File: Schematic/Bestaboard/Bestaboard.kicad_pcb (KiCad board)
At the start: 4 copper layers, 60 x 88 mm, 30 parts, among them J1 S5B-XH-A, J2 S5B-XH-A, J3 PPTC051LGBN-RC, J5 PPTC061LGBN-RC, J6 PRPC006SGAN-M71RC, J7 S3B-XH-A, J8 S3B-XH-A, J9 PRPC005SGAN-M71RC, U1 CD74HCT164E, U10 SN74HC32N, U2 CD4042BE, U3 CD4042BE, U4 SN74HC00N, U5 CD4081BE, U8 ULN2003APG, U9 ULN2003APG

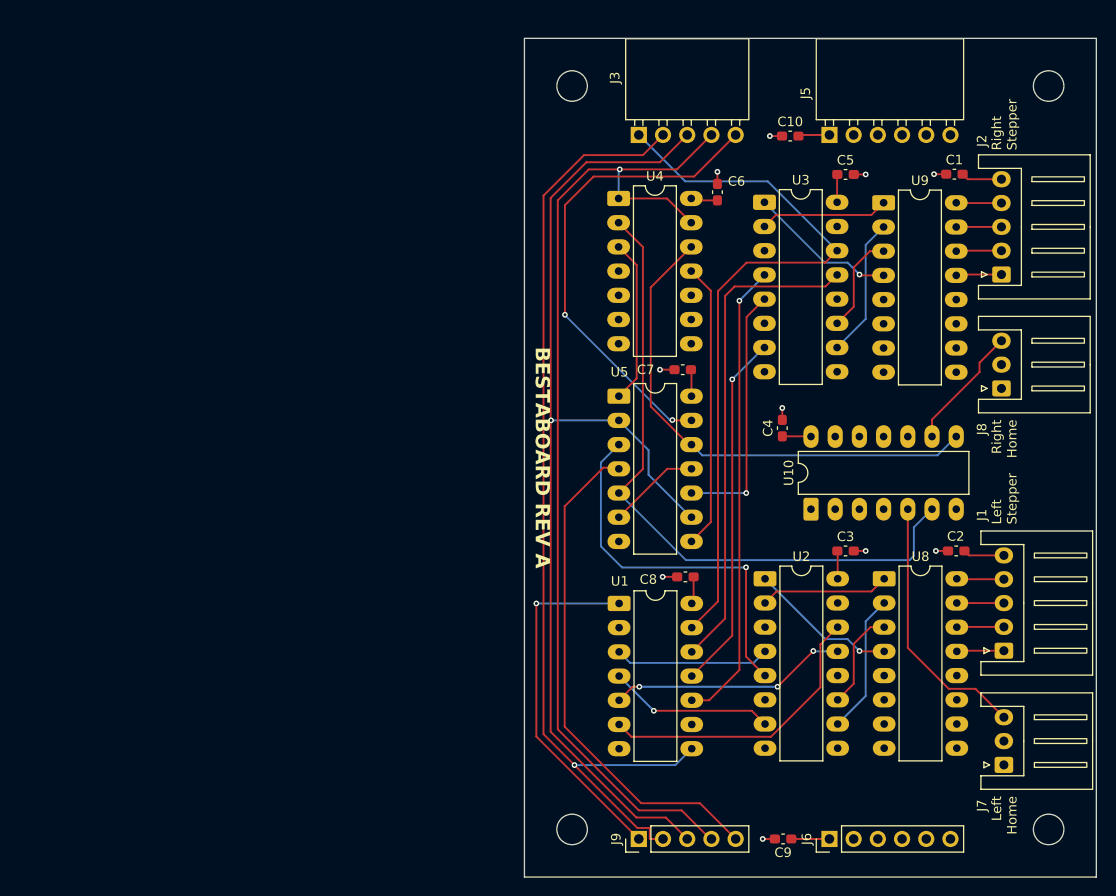
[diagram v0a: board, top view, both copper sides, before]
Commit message: Prints, Schematic, PCB, Code Update
Prints - Created print plates for flips, drum and frame, updated frame to have mounting holes on the bottom.
PCB/Schematic - Changed to 14 pin NAND chip, updated parameters.
Code - Changed code to alternate between homing and character rotation.
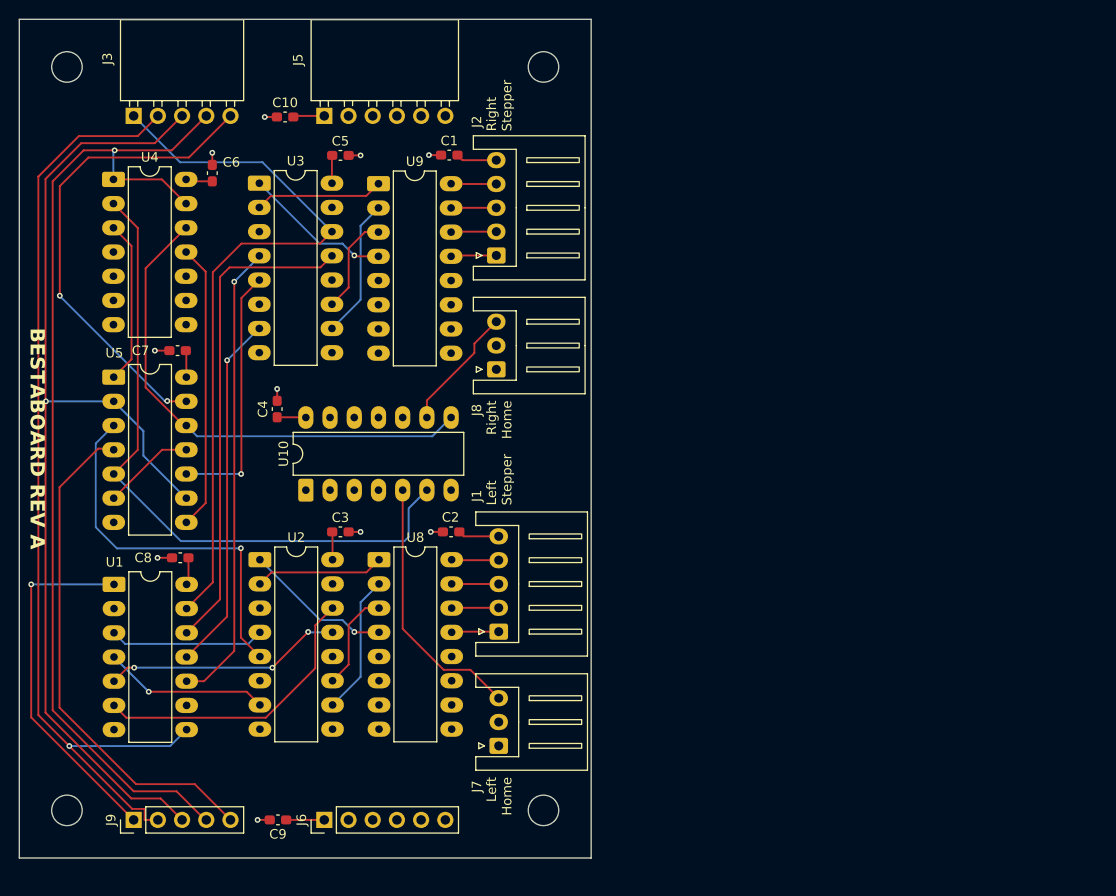
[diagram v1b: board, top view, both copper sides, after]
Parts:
- U10: value SN74HC32N -> TC74HC04APF
- U8, U9: value ULN2003APG -> ULN2003A
- moved C1 53.0 mm to (95.1, 64.2)
- moved J2 53.0 mm to (100.0, 74.8)
- moved J8 53.0 mm to (100.0, 86.7)
- moved C2 53.0 mm to (95.3, 103.8)
- moved C3 53.0 mm to (83.7, 103.8)
- moved C4 53.0 mm to (77.1, 90.9)
- moved C5 53.0 mm to (83.7, 64.3)
- moved C6 53.0 mm to (70.2, 66.1)
- moved C7 53.0 mm to (66.6, 84.8)
- moved C8 53.0 mm to (66.9, 106.5)
- moved H1 53.0 mm to (55.0, 55.0)
- moved H2 53.0 mm to (105.0, 55.0)
- moved H3 53.0 mm to (105.0, 133.0)
- moved H4 53.0 mm to (55.0, 133.0)
- moved J1 53.0 mm to (100.3, 114.2)
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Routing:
- added copper zone on In2.Cu, net +5V
- added copper zone on In1.Cu, net GND
- removed copper zone on In1.Cu, net +5V
- removed copper zone on In2.Cu, net GND
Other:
- board text added: "0"
- board text added: "0 mm"
- board text added: "0.0000 mm / 0.0000 mm"
- board text added: "0.01 mm"
- board text added: "0.02"
- board text added: "0.035 mm"
- board text added: "0.1 mm"
- board text added: "0.3000 mm"
- board text added: "1"
- board text added: "1.24 mm"
- board text added: "1.6000 mm"
- board text added: "3.3"
- board text added: "4"
- board text added: "4.5"
- board text added: "60.0000 mm x 88.0000 mm"
- board text added: "B.Cu"
- board text added: "B.Mask"
- board text added: "B.Paste"
- board text added: "B.Silkscreen"
- board text added: "BOARD CHARACTERISTICS"
- board text added: "Board Thickness:"
- board text added: "Board overall dimensions:"
- board text added: "Bottom Silk Screen"
- board text added: "Bottom Solder Mask"
- board text added: "Bottom Solder Paste"
- board text added: "Castellated pads:"
- board text added: "Color"
- board text added: "Copper Finish:"
- board text added: "Copper Layer Count:"
- board text added: "Dielectric"
- board text added: "Edge card connectors:"
- board text added: "Epsilon R"
- board text added: "F.Cu"
- board text added: "F.Mask"
- board text added: "F.Paste"
- board text added: "F.Silkscreen"
- board text added: "FR4"
- board text added: "FR4 natural"
- board text added: "Green"
- board text added: "Impedance Control:"
- board text added: "In1.Cu"
- board text added: "In2.Cu"
- board text added: "Layer Name"
- board text added: "Loss Tangent"
- board text added: "Material"
- board text added: "Min hole diameter:"
- board text added: "Min track/spacing:"
- board text added: "No"
- board text added: "None"
- board text added: "Not specified"
- board text added: "Plated Board Edge:"
- board text added: "Thickness (mm)"
- board text added: "Top Silk Screen"
- board text added: "Top Solder Mask"
- board text added: "Top Solder Paste"
- board text added: "Type"
- board text added: "White"
- board text added: "copper"
- board text added: "core"
- board text added: "prepreg"

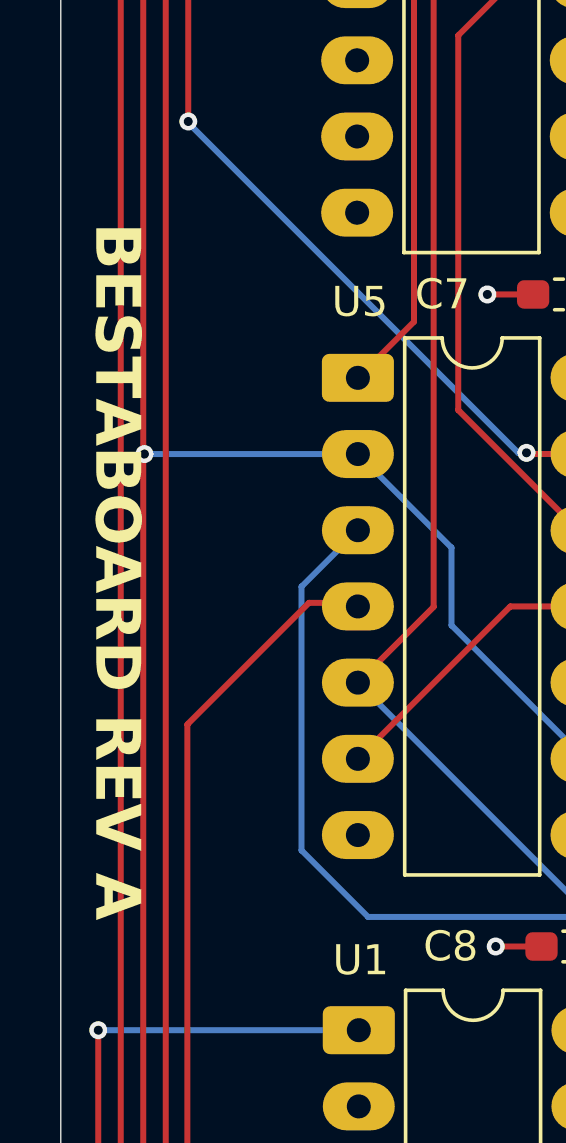
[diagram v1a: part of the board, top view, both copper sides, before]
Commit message: PCB Board Ordered vA
Board and schematic ordered to match this repo.
Continued work on 3D model to increase size of drum.
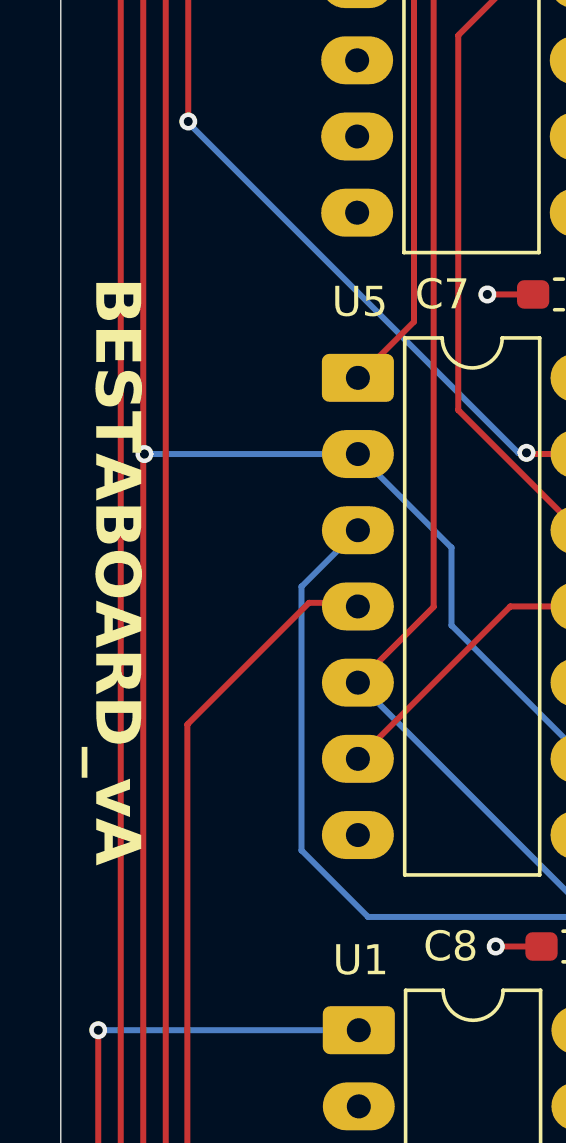
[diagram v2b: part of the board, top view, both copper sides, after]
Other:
- board text added: "BESTABOARD_vA"
- board text removed: "BESTABOARD REV A"
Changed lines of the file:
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@@
 	(generator_version "9.0")
 	(general
-		(thickness 1.6)
+		(thickness 1.600198)
 		(legacy_teardrops no)
 	)
@@
 		(6 "In2.Cu" signal)
 		(2 "B.Cu" signal)
-		(9 "F.Adhes" user "F.Adhesive")
-		(11 "B.Adhes" user "B.Adhesive")
 		(13 "F.Paste" user)
 		(15 "B.Paste" user)
-		(5 "F.SilkS" user "F.Silkscreen")
-		(7 "B.SilkS" user "B.Silkscreen")
+		(5 "F.SilkS" user "F.SilkScreen")
+		(7 "B.SilkS" user "B.SilkScreen")
 		(1 "F.Mask" user)
 		(3 "B.Mask" user)
-		(17 "Dwgs.User" user "User.Drawings")
-		(19 "Cmts.User" user "User.Comments")
-		(21 "Eco1.User" user "User.Eco1")
-		(23 "Eco2.User" user "User.Eco2")
 		(25 "Edge.Cuts" user)
 		(27 "Margin" user)
-		(31 "F.CrtYd" user "F.Courtyard")
-		(29 "B.CrtYd" user "B.Courtyard")
+		(31 "F.CrtYd" user)
+		(29 "B.CrtYd" user)
 		(35 "F.Fab" user)
-		(33 "B.Fab" user)
-		(39 "User.1" user)
-		(41 "User.2" user)
-		(43 "User.3" user)
-		(45 "User.4" user)
 	)
 	(setup
@@
 			(layer "F.SilkS"
 				(type "Top Silk Screen")
-				(color "White")
 			)
 			(layer "F.Paste"
@@
 			(layer "F.Mask"
 				(type "Top Solder Mask")
-				(color "Green")
 				(thickness 0.01)
 			)
@@
 			)
 			(layer "dielectric 1"
-				(type "prepreg")
-				(color "FR4 natural")
-				(thickness 0.1)
+				(type "core")
+				(thickness 0.480066)
 				(material "FR4")
 				(epsilon_r 4.5)
@@
 			)
 			(layer "dielectric 2"
-				(type "core")
-				(color "FR4 natural")
-				(thickness 1.24)
+				(type "prepreg")
+				(thickness 0.480066)
 				(material "FR4")
 				(epsilon_r 4.5)
@@
 			)
 			(layer "dielectric 3"
-				(type "prepreg")
-				(color "FR4 natural")
-				(thickness 0.1)
+				(type "core")
+				(thickness 0.480066)
 				(material "FR4")
 				(epsilon_r 4.5)
@@
 			(layer "B.Mask"
 				(type "Bottom Solder Mask")
-				(color "Green")
 				(thickness 0.01)
 			)
@@
 			(layer "B.SilkS"
 				(type "Bottom Silk Screen")
-				(color "White")
 			)
 			(copper_finish "None")
@@
 		)
 		(pad_to_mask_clearance 0)
+		(solder_mask_min_width 0.1016)
 		(allow_soldermask_bridges_in_footprints no)
 		(tenting front back)
@@
 			(plot_on_all_layers_selection 0x00000000_00000000_00000000_00000000)
 			(disableapertmacros no)
-			(usegerberextensions no)
+			(usegerberextensions yes)
 			(usegerberattributes yes)
 			(usegerberadvancedattributes yes)
-			(creategerberjobfile yes)
+			(creategerberjobfile no)
 			(dashed_line_dash_ratio 12.000000)
 			(dashed_line_gap_ratio 3.000000)
@@
 			(outputformat 1)
 			(mirror no)
-			(drillshape 1)
+			(drillshape 0)
 			(scaleselection 1)
-			(outputdirectory "")
+			(outputdirectory "../Drill/")
 		)
 	)
@@
 		)
 	)
-	(gr_text "BESTABOARD REV A"
+	(gr_text "BESTABOARD_vA"
 		(at 51 94 270)
 		(layer "F.SilkS")
